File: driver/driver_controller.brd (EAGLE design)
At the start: 100 x 80 mm, 36 parts, among them IC1 FT232RL, U1 STM32F10XRXT6

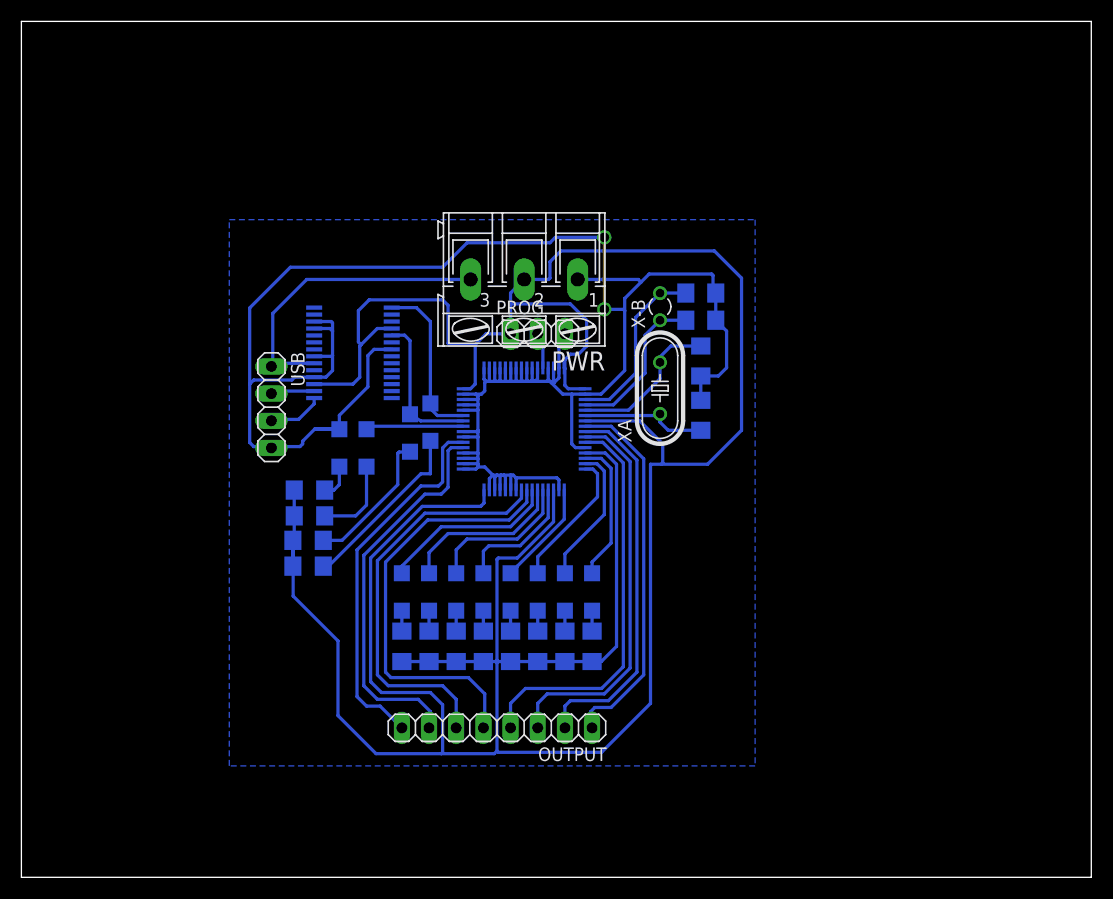
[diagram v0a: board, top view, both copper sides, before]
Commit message: ganti pake mini USB
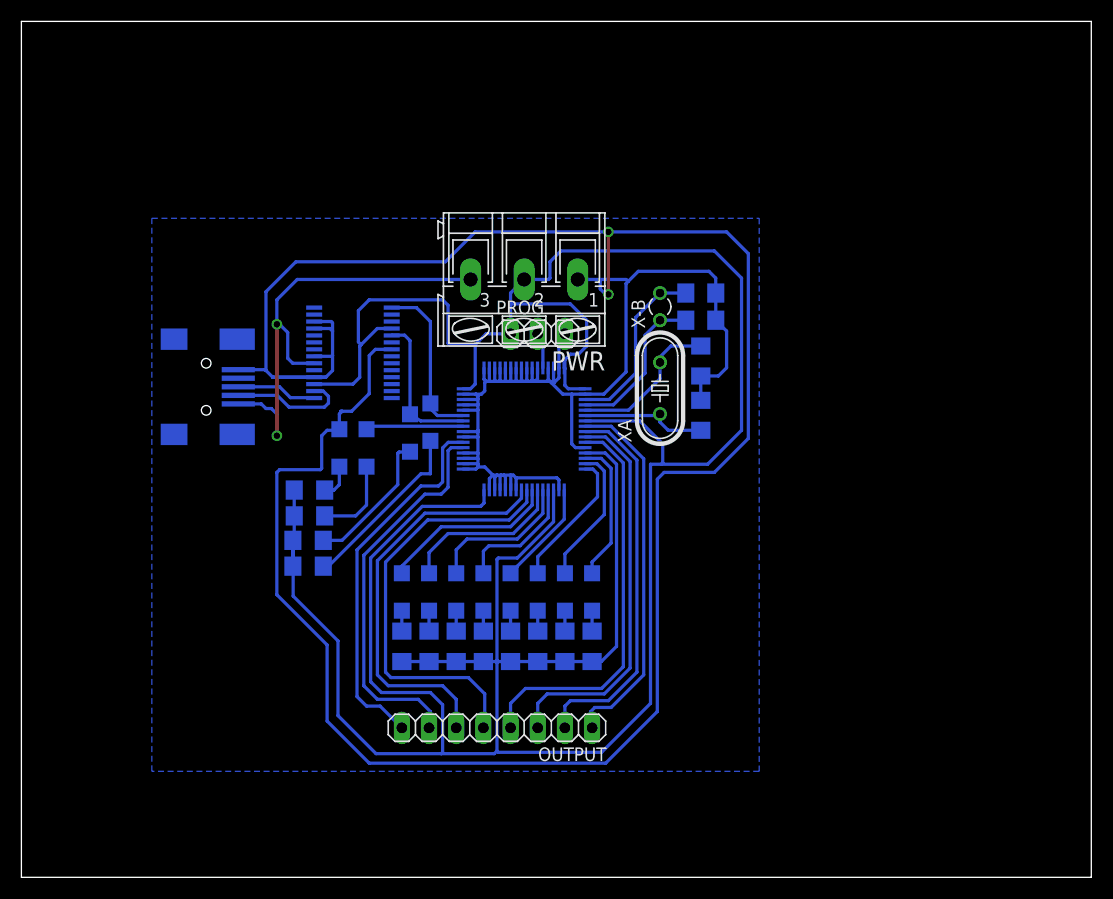
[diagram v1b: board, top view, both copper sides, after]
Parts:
- USB: value (none) -> MINI-USB-32005-201; device pinhead:1X04 -> con-cypressindustries:32005-201
- moved USB 6.39 mm to (17.3, 45.8), flipped to the bottom, turned to 180 degrees
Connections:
- net VSS: now also USB.5; no longer USB.4
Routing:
- net VSS: track 217.2 -> 335.8 mm
- net VCC: track 28.9 -> 44.0 mm, vias 0 -> 2
- net DM: track 4.09 -> 11.2 mm
- net DP: track 5.19 -> 7.53 mm

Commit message: progress 2
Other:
- board outline removed
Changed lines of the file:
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@@
 <grid distance="0.005" unitdist="inch" unit="inch" style="lines" multiple="1" display="no" altdistance="0.025" altunitdist="inch" altunit="inch"/>
 <layers>
-<layer number="1" name="Top" color="4" fill="1" visible="yes" active="yes"/>
+<layer number="1" name="Top" color="4" fill="1" visible="no" active="yes"/>
 <layer number="16" name="Bottom" color="1" fill="1" visible="yes" active="yes"/>
 <layer number="17" name="Pads" color="2" fill="1" visible="yes" active="yes"/>
 <layer number="18" name="Vias" color="14" fill="1" visible="yes" active="yes"/>
-<layer number="19" name="Unrouted" color="6" fill="1" visible="yes" active="yes"/>
-<layer number="20" name="Dimension" color="15" fill="1" visible="yes" active="yes"/>
+<layer number="19" name="Unrouted" color="6" fill="1" visible="no" active="yes"/>
+<layer number="20" name="Dimension" color="15" fill="1" visible="no" active="yes"/>
 <layer number="21" name="tPlace" color="7" fill="1" visible="no" active="yes"/>
 <layer number="22" name="bPlace" color="7" fill="1" visible="no" active="yes"/>
-<layer number="23" name="tOrigins" color="15" fill="1" visible="yes" active="yes"/>
-<layer number="24" name="bOrigins" color="15" fill="1" visible="yes" active="yes"/>
+<layer number="23" name="tOrigins" color="15" fill="1" visible="no" active="yes"/>
+<layer number="24" name="bOrigins" color="15" fill="1" visible="no" active="yes"/>
 <layer number="25" name="tNames" color="7" fill="1" visible="no" active="yes"/>
 <layer number="26" name="bNames" color="7" fill="1" visible="no" active="yes"/>
@@
 <board>
 <plain>
-<wire x1="0" y1="0" x2="100" y2="0" width="0" layer="20"/>
-<wire x1="100" y1="0" x2="100" y2="80" width="0" layer="20"/>
-<wire x1="100" y1="80" x2="0" y2="80" width="0" layer="20"/>
-<wire x1="0" y1="80" x2="0" y2="0" width="0" layer="20"/>
 </plain>
 <attributes>
